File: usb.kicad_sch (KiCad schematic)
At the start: 24 parts, among them J4 CONN_02X03, U1 LFE5U-85F-6BG381C, U6 FT231XQ, Y1 FNETHE025

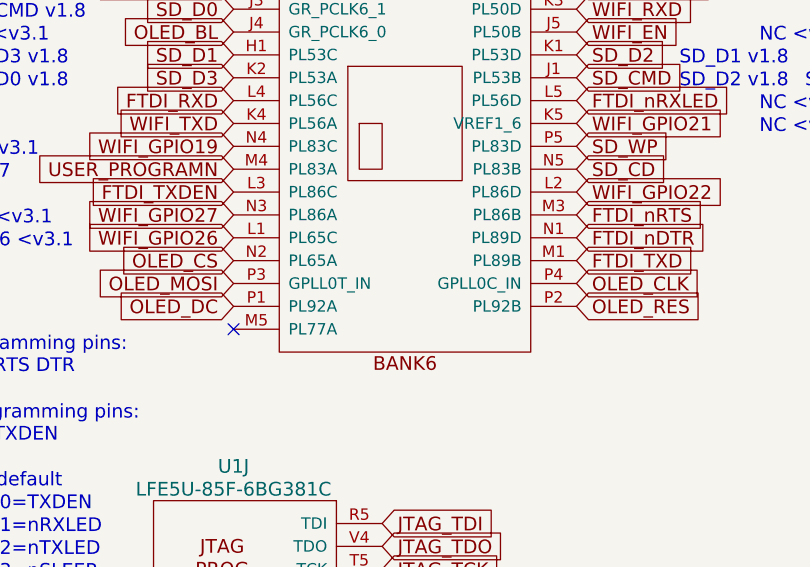
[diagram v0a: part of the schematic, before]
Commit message: remove unneeded components from schema
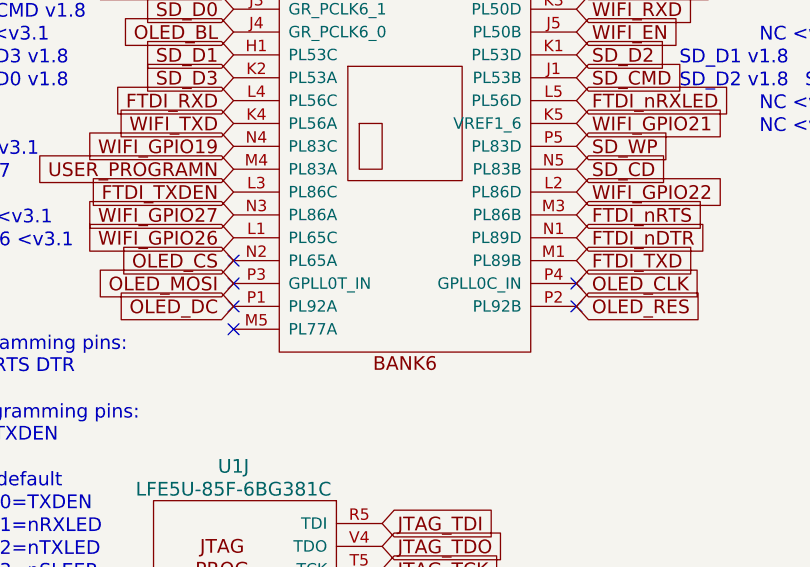
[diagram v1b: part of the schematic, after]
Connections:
- no-connect marks 2 -> 7
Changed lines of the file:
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@@
+	)
+	(no_connect
+		(at 219.71 69.85)
+	)
+	(no_connect
+		(at 219.71 67.31)
 	)
 	(no_connect
@@
 	)
 	(no_connect
+		(at 219.71 72.39)
+	)
+	(no_connect
+		(at 257.81 69.85)
+	)
+	(no_connect
 		(at 219.71 74.93)
 	)
+	(no_connect
+		(at 257.81 72.39)
+	)
 	(polyline

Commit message: start to normalize bom
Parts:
- AE1, D9, J4: now left out of the parts list
- D21: Digikey (none) -> BZT52C3V6S-TPMSCT-ND; LCSC (none) -> C353525
- D23, D24, D25: Chip1stop (none) -> C1S541901230010; Digikey (none) -> 1N914BWSCT-ND; LCSC (none) -> C258181; MPN (none) -> 1N4148WS
- D26: Chip1stop (none) -> C1S541901230010; Digikey (none) -> 1N914BWSCT-ND; LCSC (none) -> C258181
- R50, R52, R53: Digikey (none) -> 311-27.0HRCT-ND; LCSC (none) -> C325726
- R63, R64: Digikey (none) -> YAG3569CT-ND; LCSC (none) -> C217750; MPN (none) -> RC0603FR-0715KL
- U1: Digikey (none) -> 220-2177-ND; LCSC (none) -> C446029
- US2: Digikey (none) -> 609-4613-1-ND; LCSC (none) -> C132564; MPN (none) -> 10118192-0001LF

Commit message: updating part numbers across schematcs
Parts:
- D20, D21: MPN BZT52C3V6S -> 833-BZT52C3V6S-TP
- D23, D24, D25: MPN 1N4148WS -> 1N4148WS
- R40, R54: Digikey (none) -> 13-AC0603FR-071K1LCT-ND; MPN (none) -> 13-AC0603FR-071K1LCT-ND
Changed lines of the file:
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@@
 			)
 		)
+		(property "Digikey" "13-AC0603FR-071K1LCT-ND"
+			(at 57.15 118.11 90)
+			(effects
+				(font
+					(size 1.27 1.27)
+				)
+				(hide yes)
+			)
+		)
+		(property "MPN" "13-AC0603FR-071K1LCT-ND"
+			(at 57.15 118.11 90)
+			(effects
+				(font
+					(size 1.27 1.27)
+				)
+				(hide yes)
+			)
+		)
 		(pin "1"
 		)
@@
 			)
 		)
-		(property "MPN" "BZT52C3V6S"
+		(property "MPN" "833-BZT52C3V6S-TP"
 			(at 66.04 76.2 0)
 			(effects
@@
 			)
 		)
-		(property "MPN" "BZT52C3V6S"
+		(property "MPN" "833-BZT52C3V6S-TP"
 			(at 68.58 76.2 0)
 			(effects
@@
 			)
 		)
+		(property "Digikey" "13-AC0603FR-071K1LCT-ND"
+			(at 57.15 133.35 90)
+			(effects
+				(font
+					(size 1.27 1.27)
+				)
+				(hide yes)
+			)
+		)
+		(property "MPN" "13-AC0603FR-071K1LCT-ND"
+			(at 57.15 133.35 90)
+			(effects
+				(font
+					(size 1.27 1.27)
+				)
+				(hide yes)
+			)
+		)
 		(pin "1"
 		)
@@
 			)
 		)
-		(property "MPN" "1N4148WS "
+		(property "MPN" "1N4148WS"
 			(at 49.53 123.19 0)
 			(effects
@@
 			)
 		)
-		(property "MPN" "1N4148WS "
+		(property "MPN" "1N4148WS"
 			(at 49.53 138.43 0)
 			(effects
@@
 			)
 		)
-		(property "MPN" "1N4148WS "
+		(property "MPN" "1N4148WS"
 			(at 49.53 118.11 0)
 			(effects

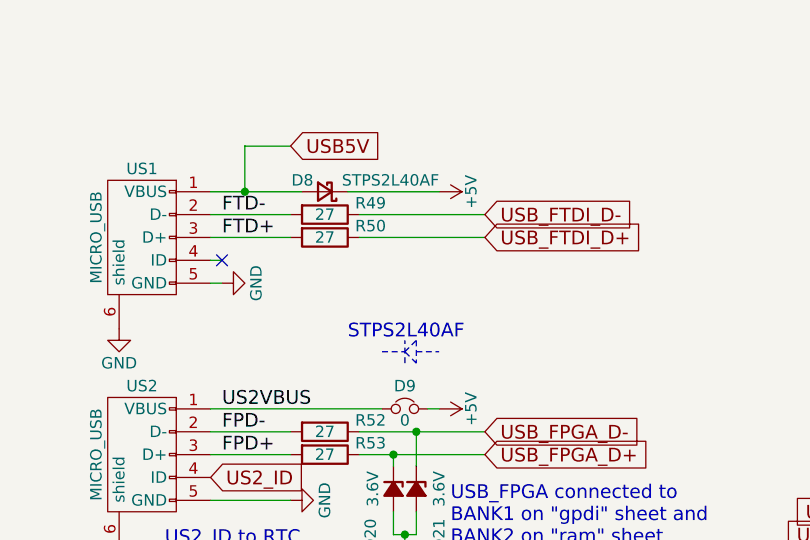
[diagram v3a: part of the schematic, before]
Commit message: switched from STPS2L30AF to STPS2L30A
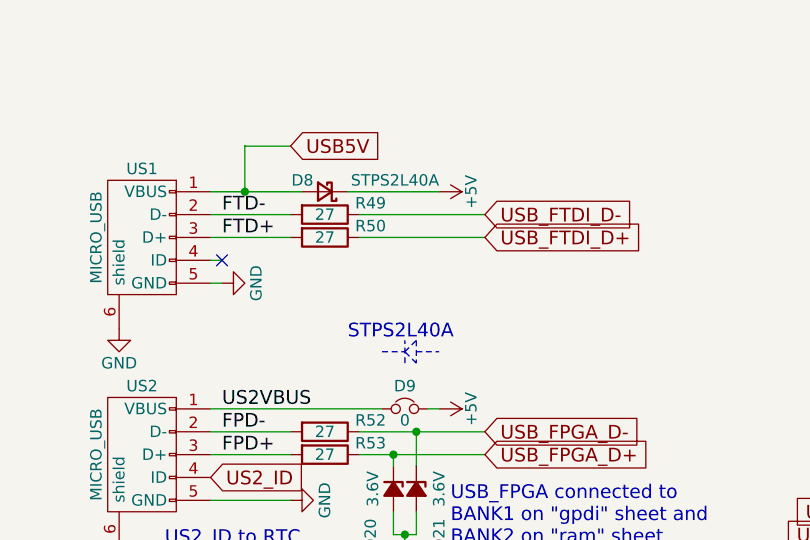
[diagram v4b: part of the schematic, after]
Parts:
- D8: value STPS2L40AF -> STPS2L40A; Digikey 497-12310-1-ND -> 497-3759-1-ND; LCSC C111630 -> (none); MPN STPS2L30AF -> 511-STPS2L30A
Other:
- note added: "STPS2L40A"
- note removed: "STPS2L40AF"
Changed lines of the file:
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@@
 		)
 	)
-	(text "STPS2L40AF"
+	(text "STPS2L40A"
 		(exclude_from_sim no)
 		(at 60.96 59.69 0)
@@
 			)
 		)
-		(property "Value" "STPS2L40AF"
+		(property "Value" "STPS2L40A"
 			(at 71.12 41.91 0)
 			(effects
@@
 			)
 		)
-		(property "MPN" "STPS2L30AF"
+		(property "MPN" "511-STPS2L30A"
 			(at 58.42 43.18 0)
 			(effects
@@
 			)
 		)
-		(property "Digikey" "497-12310-1-ND"
+		(property "Digikey" "497-3759-1-ND"
 			(at 58.42 43.18 0)
 			(effects
@@
 			)
 		)
-		(property "LCSC" "C111630"
+		(property "LCSC" ""
 			(at 58.42 43.18 0)
 			(effects

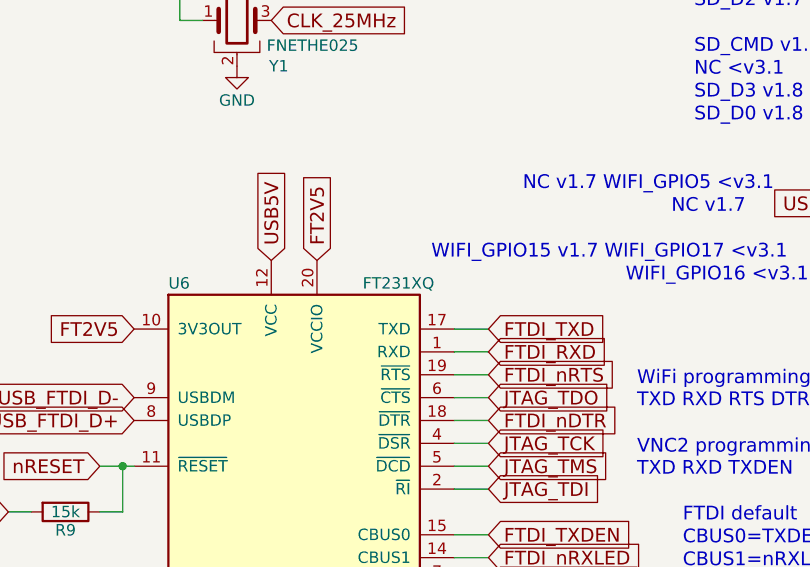
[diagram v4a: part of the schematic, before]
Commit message: switch to FT231XS (not Q) - rewire for SSOP-20
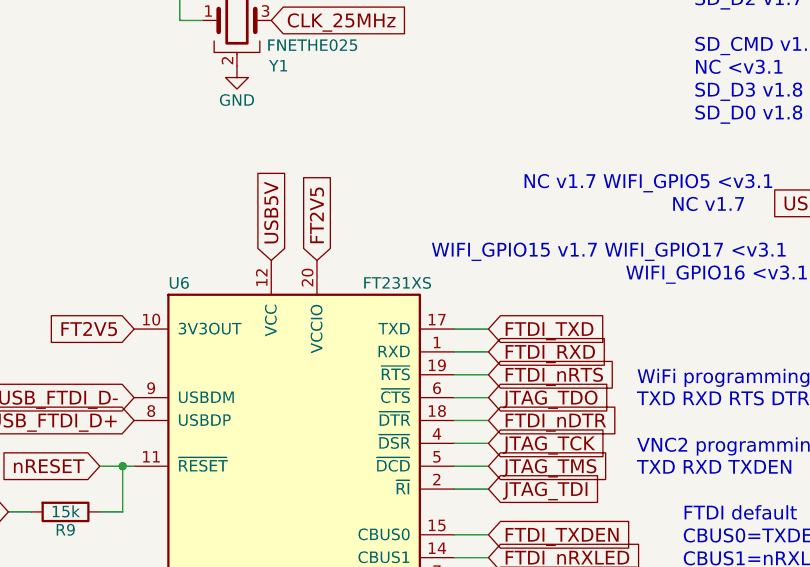
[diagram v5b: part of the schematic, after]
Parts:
- U6: value FT231XQ -> FT231XS; footprint ft231x:FT231X-QFN-20-1EP_4x4mm_P0.5mm_EP2x2mm -> ft231x:FT231X-SSOP-20_4.4x6.5mm_Pitch0.65mm; Digikey 768-1128-1-ND -> 768-1156-5-ND; MPN FT231XQ -> 895-FT231XS-U
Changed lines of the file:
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@@
 			)
 		)
-		(property "Value" "FT231XQ"
+		(property "Value" "FT231XS"
 			(at 152.4 66.04 0)
 			(effects
@@
 			)
 		)
-		(property "Footprint" "ft231x:FT231X-QFN-20-1EP_4x4mm_P0.5mm_EP2x2mm"
+		(property "Footprint" "ft231x:FT231X-SSOP-20_4.4x6.5mm_Pitch0.65mm"
 			(at 144.78 86.36 0)
 			(effects
@@
 			)
 		)
-		(property "MPN" "FT231XQ"
+		(property "MPN" "895-FT231XS-U"
 			(at 144.78 86.36 0)
 			(effects
@@
 			)
 		)
-		(property "Digikey" "768-1128-1-ND"
+		(property "Digikey" " 768-1156-5-ND"
 			(at 144.78 86.36 0)
 			(effects
